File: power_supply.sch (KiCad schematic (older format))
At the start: 77 parts, among them IC1 TPS54561DPRT, Q1 BSS138APW, Q2 BSS138-7-F, U1 AP62301WU-7, U2 AP62301WU-7, U3 AP62301WU-7, U4 74LVC1G123GN

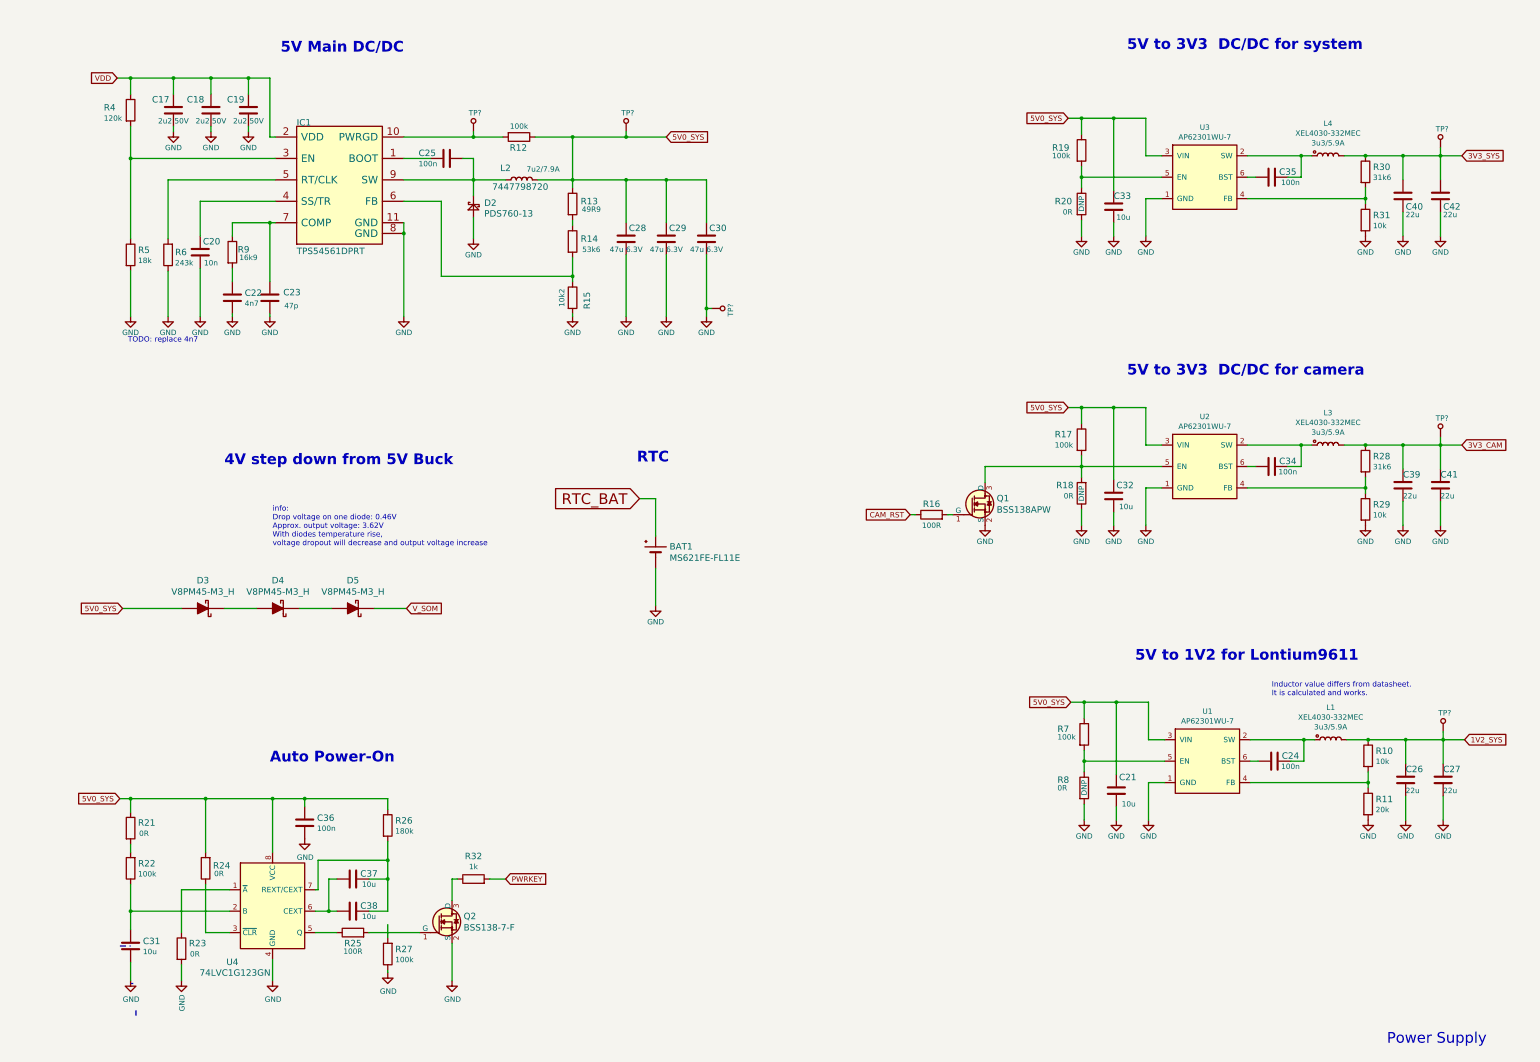
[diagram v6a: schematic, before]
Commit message: Corrected power supplies. Change of TP to 1,5mm
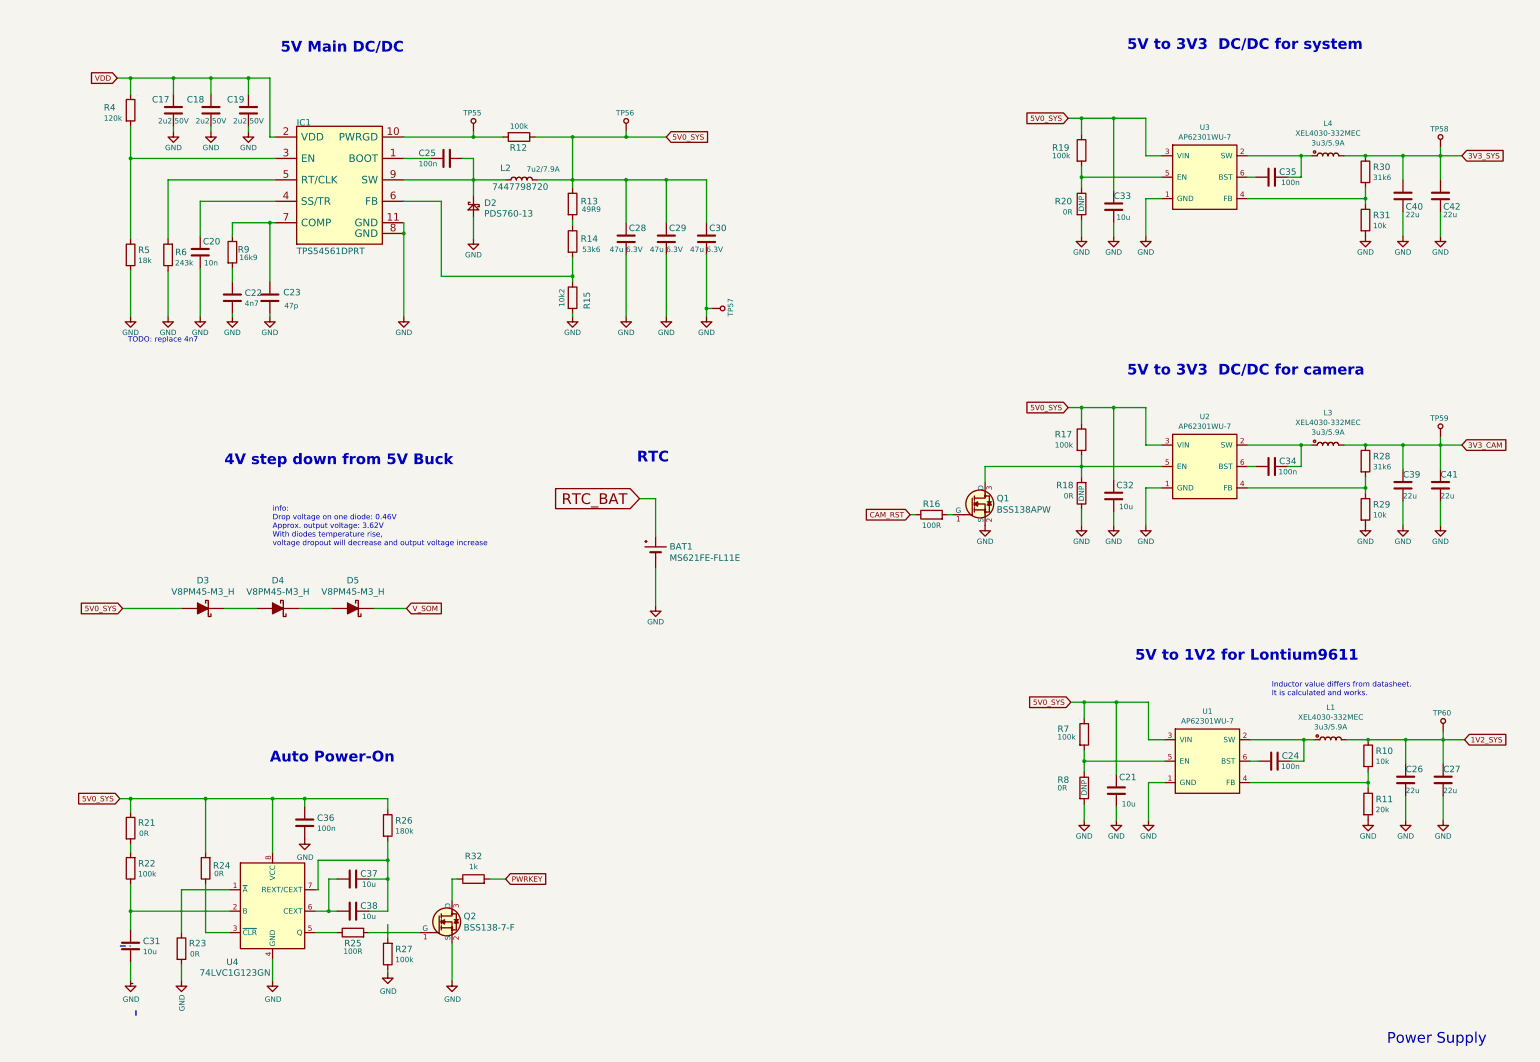
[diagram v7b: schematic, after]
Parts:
- TP55, TP56, TP57, TP58, TP59, TP60: renamed from TP?; value TP_SMD_0_75MM -> TP_SMD_1_5MM; footprint sc606-baseboard-footprints:Testpoint_smd_0_75mm -> sc606-baseboard-footprints:TP-R-1.5
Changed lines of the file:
@@
 	6975 2950 6975 3450
 $Comp
-L sc606-baseboard:GND #PWR?
+L sc606-baseboard:GND #PWR0205
 U 1 1 62F072A9
 P 6600 3525
-F 0 "#PWR?" H 6600 3275 50  0001 C CNN
+F 0 "#PWR0205" H 6600 3275 50  0001 C CNN
 F 1 "GND" H 6600 3375 50  0000 C CNN
 F 2 "" H 6600 3525 50  0001 C CNN
@@
 $EndComp
 $Comp
-L sc606-baseboard:GND #PWR?
+L sc606-baseboard:GND #PWR0206
 U 1 1 62F07484
 P 6975 3525
-F 0 "#PWR?" H 6975 3275 50  0001 C CNN
+F 0 "#PWR0206" H 6975 3275 50  0001 C CNN
 F 1 "GND" H 6975 3375 50  0000 C CNN
 F 2 "" H 6975 3525 50  0001 C CNN
@@
 $EndComp
 $Comp
-L sc606-baseboard:GND #PWR?
+L sc606-baseboard:GND #PWR0207
 U 1 1 62F1BC84
 P 2250 3525
-F 0 "#PWR?" H 2250 3275 50  0001 C CNN
+F 0 "#PWR0207" H 2250 3275 50  0001 C CNN
 F 1 "GND" H 2250 3375 50  0000 C CNN
 F 2 "" H 2250 3525 50  0001 C CNN
@@
 	1600 1300 2000 1300
 $Comp
-L sc606-baseboard:GND #PWR?
+L sc606-baseboard:GND #PWR0208
 U 1 1 6305AA66
 P 2000 1800
-F 0 "#PWR?" H 2000 1550 50  0001 C CNN
+F 0 "#PWR0208" H 2000 1550 50  0001 C CNN
 F 1 "GND" H 2000 1650 50  0000 C CNN
 F 2 "" H 2000 1800 50  0001 C CNN
@@
 	2000 1750 2000 1800
 $Comp
-L sc606-baseboard:GND #PWR?
+L sc606-baseboard:GND #PWR0209
 U 1 1 63065FD0
 P 2350 1800
-F 0 "#PWR?" H 2350 1550 50  0001 C CNN
+F 0 "#PWR0209" H 2350 1550 50  0001 C CNN
 F 1 "GND" H 2350 1650 50  0000 C CNN
 F 2 "" H 2350 1800 50  0001 C CNN
@@
 	2350 1750 2350 1800
 $Comp
-L sc606-baseboard:GND #PWR?
+L sc606-baseboard:GND #PWR0210
 U 1 1 6306FD5C
 P 2700 1800
-F 0 "#PWR?" H 2700 1550 50  0001 C CNN
+F 0 "#PWR0210" H 2700 1550 50  0001 C CNN
 F 1 "GND" H 2700 1650 50  0000 C CNN
 F 2 "" H 2700 1800 50  0001 C CNN
@@
 P 4800 1700
 AR Path="/61D43102/63123342" Ref="TP?"  Part="1"
-AR Path="/61D49F54/63123342" Ref="TP?"  Part="1"
-F 0 "TP?" H 4725 1625 50  0000 L CNN
-F 1 "TP_SMD_0_75MM" H 4800 1600 50  0001 C CNN
-F 2 "sc606-baseboard-footprints:Testpoint_smd_0_75mm" H 5000 1900 60  0001 L CNN
+AR Path="/61D49F54/63123342" Ref="TP55"  Part="1"
+F 0 "TP55" H 4725 1625 50  0000 L CNN
+F 1 "TP_SMD_1_5MM" H 4800 1600 50  0001 C CNN
+F 2 "sc606-baseboard-footprints:TP-R-1.5" H 5000 1900 60  0001 L CNN
 F 3 "" H 5000 2000 60  0001 L CNN
 	1    4800 1700
@@
 	13475 2550 13475 2775
 $Comp
-L sc606-baseboard:GND #PWR?
+L sc606-baseboard:GND #PWR0211
 U 1 1 636A6080
 P 13825 2775
-F 0 "#PWR?" H 13825 2525 50  0001 C CNN
+F 0 "#PWR0211" H 13825 2525 50  0001 C CNN
 F 1 "GND" H 13825 2625 50  0000 C CNN
 F 2 "" H 13825 2775 50  0001 C CNN
@@
 	13825 2550 13825 2775
 $Comp
-L sc606-baseboard:GND #PWR?
+L sc606-baseboard:GND #PWR0212
 U 1 1 636BAA3B
 P 10475 2775
-F 0 "#PWR?" H 10475 2525 50  0001 C CNN
+F 0 "#PWR0212" H 10475 2525 50  0001 C CNN
 F 1 "GND" H 10475 2625 50  0000 C CNN
 F 2 "" H 10475 2775 50  0001 C CNN
@@
 5V0_SYS
 $Comp
-L sc606-baseboard:GND #PWR?
+L sc606-baseboard:GND #PWR0213
 U 1 1 637EB9BE
 P 10775 5475
-F 0 "#PWR?" H 10775 5225 50  0001 C CNN
+F 0 "#PWR0213" H 10775 5225 50  0001 C CNN
 F 1 "GND" H 10775 5325 50  0000 C CNN
 F 2 "" H 10775 5475 50  0001 C CNN
@@
 $EndComp
 $Comp
-L sc606-baseboard:GND #PWR?
+L sc606-baseboard:GND #PWR0214
 U 1 1 637EB9C4
 P 11075 5475
-F 0 "#PWR?" H 11075 5225 50  0001 C CNN
+F 0 "#PWR0214" H 11075 5225 50  0001 C CNN
 F 1 "GND" H 11075 5325 50  0000 C CNN
 F 2 "" H 11075 5475 50  0001 C CNN
@@
 	12625 4725 12525 4725
 $Comp
-L sc606-baseboard:GND #PWR?
+L sc606-baseboard:GND #PWR0215
 U 1 1 637EB9CD
 P 13125 5475
-F 0 "#PWR?" H 13125 5225 50  0001 C CNN
+F 0 "#PWR0215" H 13125 5225 50  0001 C CNN
 F 1 "GND" H 13125 5325 50  0000 C CNN
 F 2 "" H 13125 5475 50  0001 C CNN
@@
 $EndComp
 $Comp
-L sc606-baseboard:GND #PWR?
+L sc606-baseboard:GND #PWR0216
 U 1 1 637EB9D3
 P 13475 5475
-F 0 "#PWR?" H 13475 5225 50  0001 C CNN
+F 0 "#PWR0216" H 13475 5225 50  0001 C CNN
 F 1 "GND" H 13475 5325 50  0000 C CNN
 F 2 "" H 13475 5475 50  0001 C CNN
@@
 	13475 5250 13475 5475
 $Comp
-L sc606-baseboard:GND #PWR?
+L sc606-baseboard:GND #PWR0217
 U 1 1 637EBA45
 P 13825 5475
-F 0 "#PWR?" H 13825 5225 50  0001 C CNN
+F 0 "#PWR0217" H 13825 5225 50  0001 C CNN
 F 1 "GND" H 13825 5325 50  0000 C CNN
 F 2 "" H 13825 5475 50  0001 C CNN
@@
 	13825 5250 13825 5475
 $Comp
-L sc606-baseboard:GND #PWR?
+L sc606-baseboard:GND #PWR0218
 U 1 1 637EBA4C
 P 10475 5475
-F 0 "#PWR?" H 10475 5225 50  0001 C CNN
+F 0 "#PWR0218" H 10475 5225 50  0001 C CNN
 F 1 "GND" H 10475 5325 50  0000 C CNN
 F 2 "" H 10475 5475 50  0001 C CNN
@@
 5V0_SYS
 $Comp
-L sc606-baseboard:GND #PWR?
+L sc606-baseboard:GND #PWR0219
 U 1 1 638D763A
 P 10800 8225
-F 0 "#PWR?" H 10800 7975 50  0001 C CNN
+F 0 "#PWR0219" H 10800 7975 50  0001 C CNN
 F 1 "GND" H 10800 8075 50  0000 C CNN
 F 2 "" H 10800 8225 50  0001 C CNN
@@
 $EndComp
 $Comp
-L sc606-baseboard:GND #PWR?
+L sc606-baseboard:GND #PWR0220
 U 1 1 638D7640
 P 11100 8225
-F 0 "#PWR?" H 11100 7975 50  0001 C CNN
+F 0 "#PWR0220" H 11100 7975 50  0001 C CNN
 F 1 "GND" H 11100 8075 50  0000 C CNN
 F 2 "" H 11100 8225 50  0001 C CNN
@@
 	12650 7475 12550 7475
 $Comp
-L sc606-baseboard:GND #PWR?
+L sc606-baseboard:GND #PWR0221
 U 1 1 638D7649
 P 13150 8225
-F 0 "#PWR?" H 13150 7975 50  0001 C CNN
+F 0 "#PWR0221" H 13150 7975 50  0001 C CNN
 F 1 "GND" H 13150 8075 50  0000 C CNN
 F 2 "" H 13150 8225 50  0001 C CNN
@@
 $EndComp
 $Comp
-L sc606-baseboard:GND #PWR?
+L sc606-baseboard:GND #PWR0222
 U 1 1 638D764F
 P 13500 8225
-F 0 "#PWR?" H 13500 7975 50  0001 C CNN
+F 0 "#PWR0222" H 13500 7975 50  0001 C CNN
 F 1 "GND" H 13500 8075 50  0000 C CNN
 F 2 "" H 13500 8225 50  0001 C CNN
@@
 	13500 8000 13500 8225
 $Comp
-L sc606-baseboard:GND #PWR?
+L sc606-baseboard:GND #PWR0223
 U 1 1 638D7669
 P 13850 8225
-F 0 "#PWR?" H 13850 7975 50  0001 C CNN
+F 0 "#PWR0223" H 13850 7975 50  0001 C CNN
 F 1 "GND" H 13850 8075 50  0000 C CNN
 F 2 "" H 13850 8225 50  0001 C CNN
@@
 	13850 8000 13850 8225
 $Comp
-L sc606-baseboard:GND #PWR?
+L sc606-baseboard:GND #PWR0224
 U 1 1 638D7670
 P 10500 8225
-F 0 "#PWR?" H 10500 7975 50  0001 C CNN
+F 0 "#PWR0224" H 10500 7975 50  0001 C CNN
 F 1 "GND" H 10500 8075 50  0000 C CNN
 F 2 "" H 10500 8225 50  0001 C CNN
@@
 P 6225 1700
 AR Path="/61D43102/63A502B9" Ref="TP?"  Part="1"
-AR Path="/61D49F54/63A502B9" Ref="TP?"  Part="1"
-F 0 "TP?" H 6150 1625 50  0000 L CNN
-F 1 "TP_SMD_0_75MM" H 6225 1600 50  0001 C CNN
-F 2 "sc606-baseboard-footprints:Testpoint_smd_0_75mm" H 6425 1900 60  0001 L CNN
+AR Path="/61D49F54/63A502B9" Ref="TP56"  Part="1"
+F 0 "TP56" H 6150 1625 50  0000 L CNN
+F 1 "TP_SMD_1_5MM" H 6225 1600 50  0001 C CNN
+F 2 "sc606-baseboard-footprints:TP-R-1.5" H 6425 1900 60  0001 L CNN
 F 3 "" H 6425 2000 60  0001 L CNN
 	1    6225 1700
@@
 P 7125 3450
 AR Path="/61D43102/63A6A526" Ref="TP?"  Part="1"
-AR Path="/61D49F54/63A6A526" Ref="TP?"  Part="1"
-F 0 "TP?" H 7050 3375 50  0000 L CNN
-F 1 "TP_SMD_0_75MM" H 7125 3350 50  0001 C CNN
-F 2 "sc606-baseboard-footprints:Testpoint_smd_0_75mm" H 7325 3650 60  0001 L CNN
+AR Path="/61D49F54/63A6A526" Ref="TP57"  Part="1"
+F 0 "TP57" H 7050 3375 50  0000 L CNN
+F 1 "TP_SMD_1_5MM" H 7125 3350 50  0001 C CNN
+F 2 "sc606-baseboard-footprints:TP-R-1.5" H 7325 3650 60  0001 L CNN
 F 3 "" H 7325 3750 60  0001 L CNN
 	1    7125 3450
@@
 P 13825 1850
 AR Path="/61D43102/63A844BE" Ref="TP?"  Part="1"
-AR Path="/61D49F54/63A844BE" Ref="TP?"  Part="1"
-F 0 "TP?" H 13750 1775 50  0000 L CNN
-F 1 "TP_SMD_0_75MM" H 13825 1750 50  0001 C CNN
-F 2 "sc606-baseboard-footprints:Testpoint_smd_0_75mm" H 14025 2050 60  0001 L CNN
+AR Path="/61D49F54/63A844BE" Ref="TP58"  Part="1"
+F 0 "TP58" H 13750 1775 50  0000 L CNN
+F 1 "TP_SMD_1_5MM" H 13825 1750 50  0001 C CNN
+F 2 "sc606-baseboard-footprints:TP-R-1.5" H 14025 2050 60  0001 L CNN
 F 3 "" H 14025 2150 60  0001 L CNN
 	1    13825 1850
@@
 P 13825 4550
 AR Path="/61D43102/63A9E514" Ref="TP?"  Part="1"
-AR Path="/61D49F54/63A9E514" Ref="TP?"  Part="1"
-F 0 "TP?" H 13750 4475 50  0000 L CNN
-F 1 "TP_SMD_0_75MM" H 13825 4450 50  0001 C CNN
-F 2 "sc606-baseboard-footprints:Testpoint_smd_0_75mm" H 14025 4750 60  0001 L CNN
+AR Path="/61D49F54/63A9E514" Ref="TP59"  Part="1"
+F 0 "TP59" H 13750 4475 50  0000 L CNN
+F 1 "TP_SMD_1_5MM" H 13825 4450 50  0001 C CNN
+F 2 "sc606-baseboard-footprints:TP-R-1.5" H 14025 4750 60  0001 L CNN
 F 3 "" H 14025 4850 60  0001 L CNN
 	1    13825 4550
@@
 P 13850 7300
 AR Path="/61D43102/63AAD1FF" Ref="TP?"  Part="1"
-AR Path="/61D49F54/63AAD1FF" Ref="TP?"  Part="1"
-F 0 "TP?" H 13775 7225 50  0000 L CNN
-F 1 "TP_SMD_0_75MM" H 13850 7200 50  0001 C CNN
-F 2 "sc606-baseboard-footprints:Testpoint_smd_0_75mm" H 14050 7500 60  0001 L CNN
+AR Path="/61D49F54/63AAD1FF" Ref="TP60"  Part="1"
+F 0 "TP60" H 13775 7225 50  0000 L CNN
+F 1 "TP_SMD_1_5MM" H 13850 7200 50  0001 C CNN
+F 2 "sc606-baseboard-footprints:TP-R-1.5" H 14050 7500 60  0001 L CNN
 F 3 "" H 14050 7600 60  0001 L CNN
 	1    13850 7300

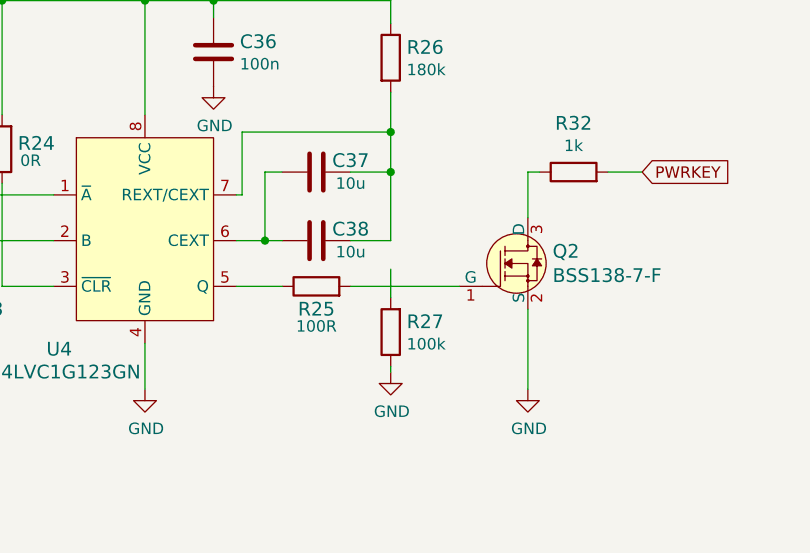
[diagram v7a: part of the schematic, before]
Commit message: Fixed DRC and other minor errors
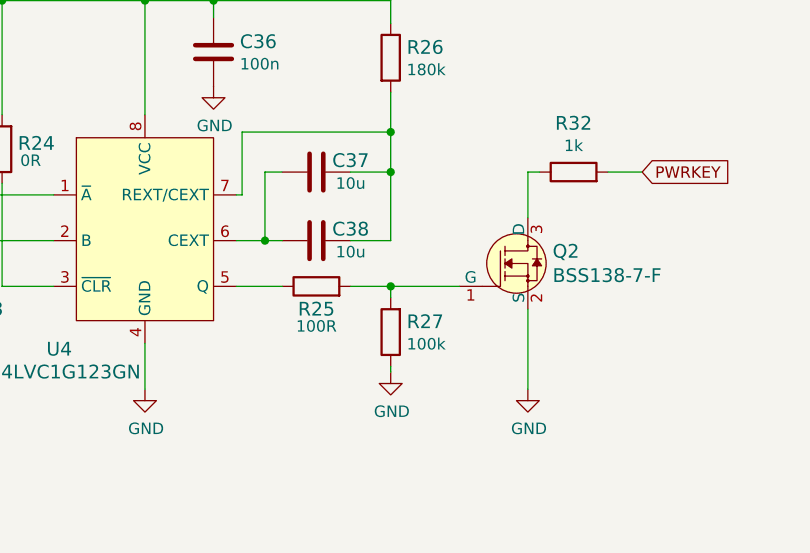
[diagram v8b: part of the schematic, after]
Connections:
- net at Q2.1 (G), R25.2: now also R27.2
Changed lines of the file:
@@
 	4000 9650 4000 9625
 Wire Wire Line
-	4000 9325 4000 9200
+	4000 9325 4000 9275
 Wire Wire Line
 	3450 9075 3450 8775
@@
 	1600 9750 1625 9750
 Wire Wire Line
-	3825 9275 4300 9275
+	3825 9275 4000 9275
 $Comp
 L sc606-baseboard:R_180k_0402 R26
@@
 	1    0    0    -1
 $EndComp
+Connection ~ 4000 9275
+Wire Wire Line
+	4000 9275 4300 9275
 $EndSCHEMATC
